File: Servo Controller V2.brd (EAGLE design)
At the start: 31.2 x 59.2 mm, 37 parts, among them P1 Power, IO, P2 Servo, P3 Program, Q1 BSS138, Q2 IRLML9301TRPBF, U1 ATTINY402-SSNR, U2 TPS82140SILR, U3 MCP1754ST-3302E_CB, U4 MCP1754ST-3302E_CB

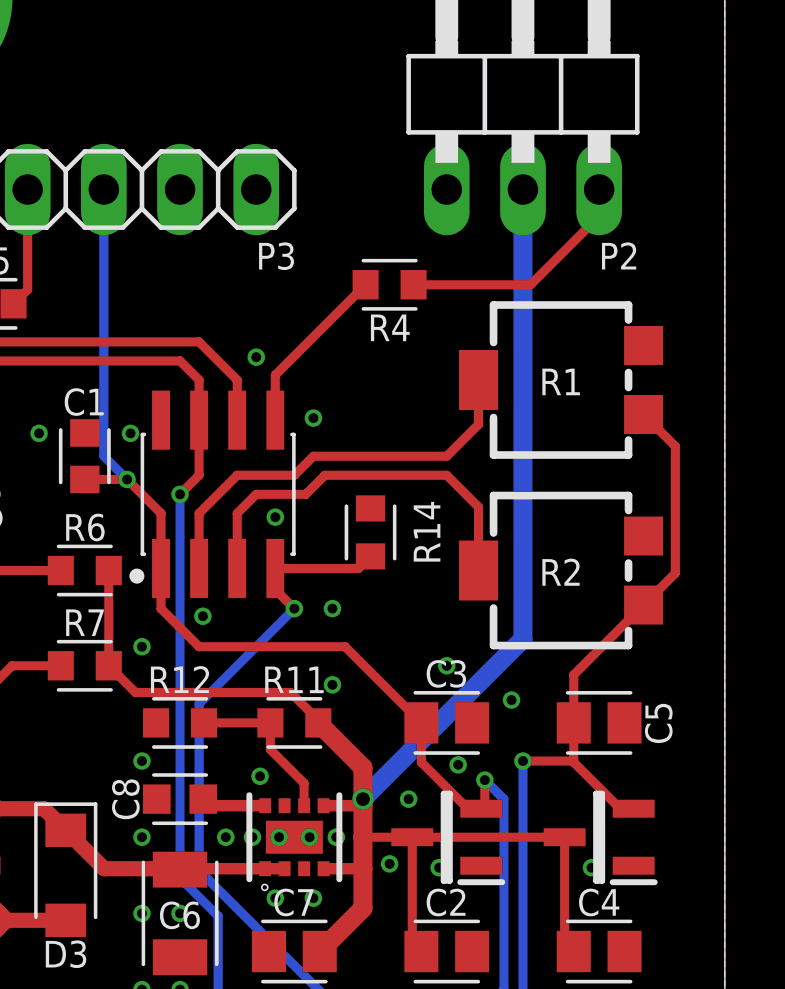
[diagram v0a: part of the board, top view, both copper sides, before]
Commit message: Eliminated back EMI on the 5V rail from a large motor braking.
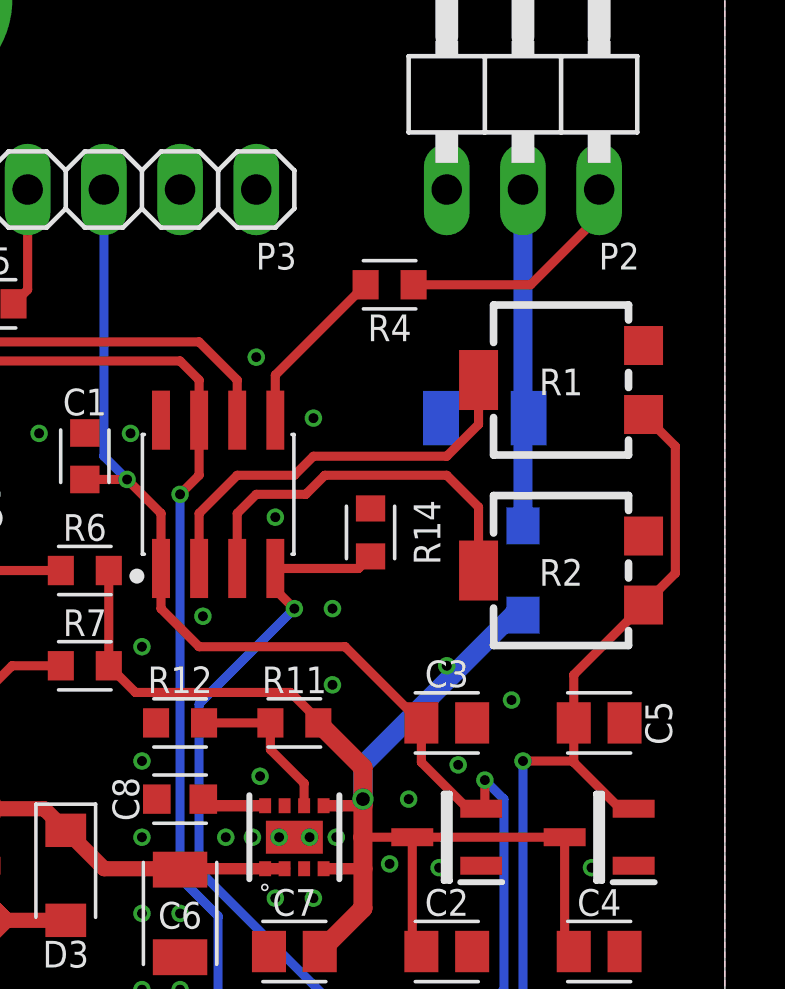
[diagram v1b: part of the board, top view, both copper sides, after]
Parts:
- added C9: 10µ 25V, lcr:CAPC3216X180
- added D4: MBR130LSFT1G, lcr:SODFL3616X98
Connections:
- new net N$19: C9.2, D4.1, P2.2
- net +5V: now also D4.2; no longer P2.2
- net GND: now also C9.1
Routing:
- net +5V: track 59.8 -> 45.8 mm
- net N$19: track 0.00 -> 11.4 mm
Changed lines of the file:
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@@
 </layers>
 <board>
+<fusionsync huburn="a.cGVyc29uYWw6dWUyYTRiMmQy" projecturn="a.cGVyc29uYWw6dWUyYTRiMmQyIzIwMTcxMjI3MTA5OTM1NzI2" f3durn="urn:adsk.wipprod:dm.lineage:PpBJHXuUREOfGaQz9pWU0A" pcbguid="c0488916-b52c-4e85-8943-ab9555ab079e" lastpulledtime="" lastsyncedchangeguid="bafbf799-f43d-3f73-44a9-28bf91460bd9"/>
 <plain>
 <wire x1="0.889" y1="-6.731" x2="32.131" y2="-6.731" width="0" layer="20"/>
@@
 </element>
 <element name="U$2" library="SparkFun-Aesthetics" library_urn="urn:adsk.eagle:library:507" package="OSHW-LOGO-MINI" package3d_urn="urn:adsk.eagle:package:37101/1" value="" x="29.21" y="45.72" smashed="yes" rot="MR0"/>
+<element name="C9" library="lcr" library_urn="urn:adsk.eagle:library:3920968" package="CAPC3216X180" package3d_urn="urn:adsk.eagle:package:4274891/1" value="10µ 25V" x="24.13" y="34.29" smashed="yes" rot="MR180">
+<attribute name="NAME" x="24.13" y="33.68569375" size="0.889" layer="26" ratio="10" rot="MR90" align="center-left"/>
+<attribute name="VALUE" x="24.13" y="36.1467" size="1.27" layer="28" rot="MR180" align="top-center"/>
+</element>
+<element name="D4" library="lcr" library_urn="urn:adsk.eagle:library:3920968" package="SODFL3616X98" package3d_urn="urn:adsk.eagle:package:4270842/1" value="MBR130LSFT1G" x="25.4" y="29.21" smashed="yes" rot="MR270">
+<attribute name="NAME" x="24.313" y="29.397" size="0.889" layer="26" ratio="10" rot="MR90" align="top-center"/>
+<attribute name="VALUE" x="26.935" y="29.21" size="1.27" layer="28" rot="MR270" align="top-center"/>
+</element>
 </elements>
 <signals>
@@
 <via x="16.637" y="22.352" extent="1-16" drill="0.3302"/>
 <via x="20.955" y="19.431" extent="1-16" drill="0.3302"/>
+<contactref element="C9" pad="1"/>
 </signal>
 <signal name="UPDI">
@@
 <contactref element="U2" pad="5"/>
 <contactref element="C7" pad="2"/>
-<contactref element="P2" pad="2"/>
 <contactref element="R6" pad="2"/>
 <contactref element="R7" pad="2"/>
 <wire x1="11.5946" y1="29.21" x2="11.5946" y2="26.035" width="0.3048" layer="1"/>
 <wire x1="21.71" y1="20.32" x2="26.79" y2="20.32" width="0.3048" layer="1"/>
-<wire x1="25.4" y1="41.91" x2="25.4" y2="26.924" width="0.635" layer="16"/>
-<wire x1="25.4" y1="26.924" x2="20.066" y2="21.59" width="0.635" layer="16"/>
+<wire x1="25.053" y1="27.72" x2="20.066" y2="22.733" width="0.635" layer="16"/>
+<wire x1="20.066" y1="21.59" x2="20.066" y2="22.733" width="0.635" layer="16"/>
+<wire x1="25.4" y1="27.72" x2="25.053" y2="27.72" width="0.635" layer="16"/>
 <via x="20.066" y="21.59" extent="1-16" drill="0.4572"/>
 <wire x1="20.066" y1="22.6436" x2="18.5796" y2="24.13" width="0.635" layer="1"/>
@@
 <wire x1="18.5796" y1="24.2194" x2="18.5796" y2="24.13" width="0.3048" layer="1"/>
 <wire x1="17.653" y1="25.146" x2="18.5796" y2="24.2194" width="0.3048" layer="1"/>
+<contactref element="D4" pad="2"/>
 </signal>
 <signal name="N$15">
@@
 <signal name="N$17">
 <via x="5.08" y="48.26" extent="1-16" drill="3.50011875" diameter="6.604"/>
+</signal>
+<signal name="N$19">
+<contactref element="P2" pad="2"/>
+<contactref element="D4" pad="1"/>
+<contactref element="C9" pad="2"/>
+<wire x1="25.4" y1="30.7" x2="25.4" y2="34.1001" width="0.635" layer="16"/>
+<wire x1="25.4" y1="34.1001" x2="25.5899" y2="34.29" width="0.635" layer="16"/>
+<wire x1="25.4" y1="41.91" x2="25.4" y2="34.4799" width="0.635" layer="16"/>
+<wire x1="25.4" y1="34.4799" x2="25.5899" y2="34.29" width="0.635" layer="16"/>
 </signal>
 </signals>
@@
 </note>
 <note version="8.3" severity="warning">
+Since Version 8.3, EAGLE supports Fusion synchronisation.
+This feature will not be available in this version and saving
+the document will break the link to the Fusion PCB feature.
+</note>
+<note version="8.3" severity="warning">

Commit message: Display OSHW logo on schematic.
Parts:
- LOGO1: value (none) -> OSHW-LOGOMINI
- renumbered U$2 to LOGO1
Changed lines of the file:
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@@
 <attribute name="VALUE" x="27.7714" y="12.7" size="1.27" layer="28" rot="MR90" align="top-center"/>
 </element>
-<element name="U$2" library="SparkFun-Aesthetics" library_urn="urn:adsk.eagle:library:507" package="OSHW-LOGO-MINI" package3d_urn="urn:adsk.eagle:package:37101/1" value="" x="29.21" y="45.72" smashed="yes" rot="MR0"/>
 <element name="C9" library="lcr" library_urn="urn:adsk.eagle:library:3920968" package="CAPC3216X180" package3d_urn="urn:adsk.eagle:package:4274891/1" value="10µ 25V" x="24.13" y="34.29" smashed="yes" rot="MR180">
 <attribute name="NAME" x="24.13" y="33.68569375" size="0.889" layer="26" ratio="10" rot="MR90" align="center-left"/>
@@
 <attribute name="VALUE" x="26.935" y="29.21" size="1.27" layer="28" rot="MR270" align="top-center"/>
 </element>
+<element name="LOGO1" library="SparkFun-Aesthetics" library_urn="urn:adsk.eagle:library:507" package="OSHW-LOGO-MINI" package3d_urn="urn:adsk.eagle:package:37101/1" value="OSHW-LOGOMINI" x="29.21" y="45.72" smashed="yes" rot="MR0"/>
 </elements>
 <signals>
